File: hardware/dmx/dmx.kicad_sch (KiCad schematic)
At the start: 67 parts, among them J1 Midi In, J2 Midi Thru, J3 NeoPixel, J4 Power, J5 DMX, J6 I2C0, J7 I2C1, Q1 BSS138, Q2 BSS138, Q3 TSM680P06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

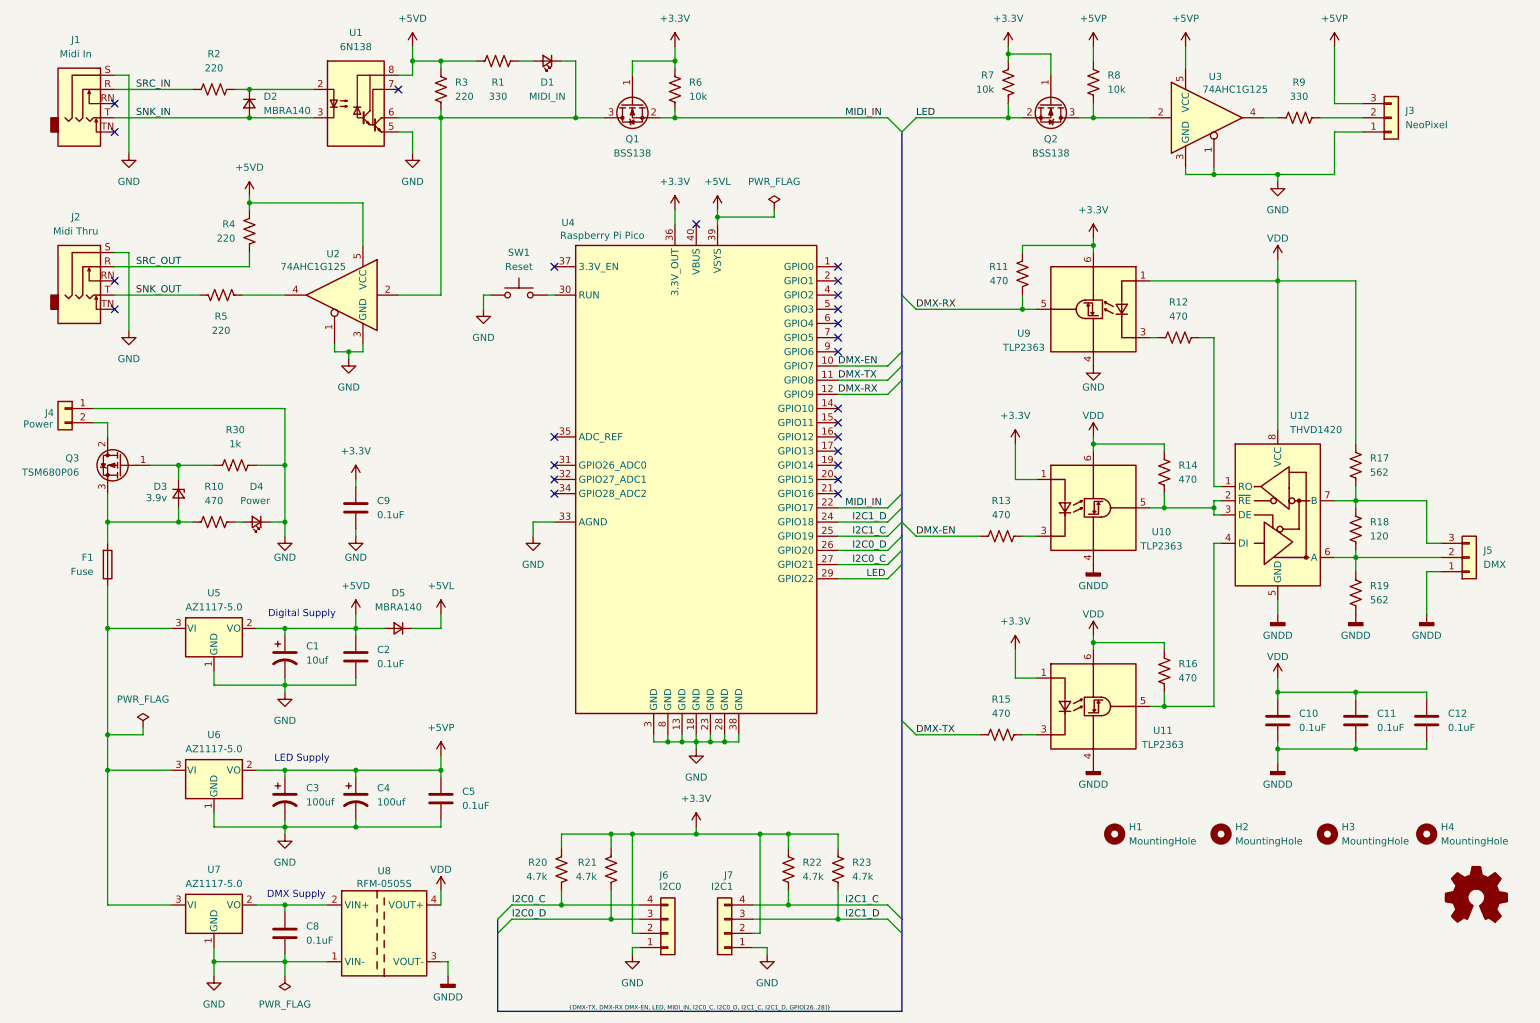
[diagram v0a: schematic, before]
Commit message: Rev 1.1: - Update to latest KiCad - Fixed short in servo board - Updates to right-angle diag connector on servo boards - Fixed microproc footprint on diag board - Flipped I2C connector to top of diag board - Pass all ERC and DRC checks, add exclusions
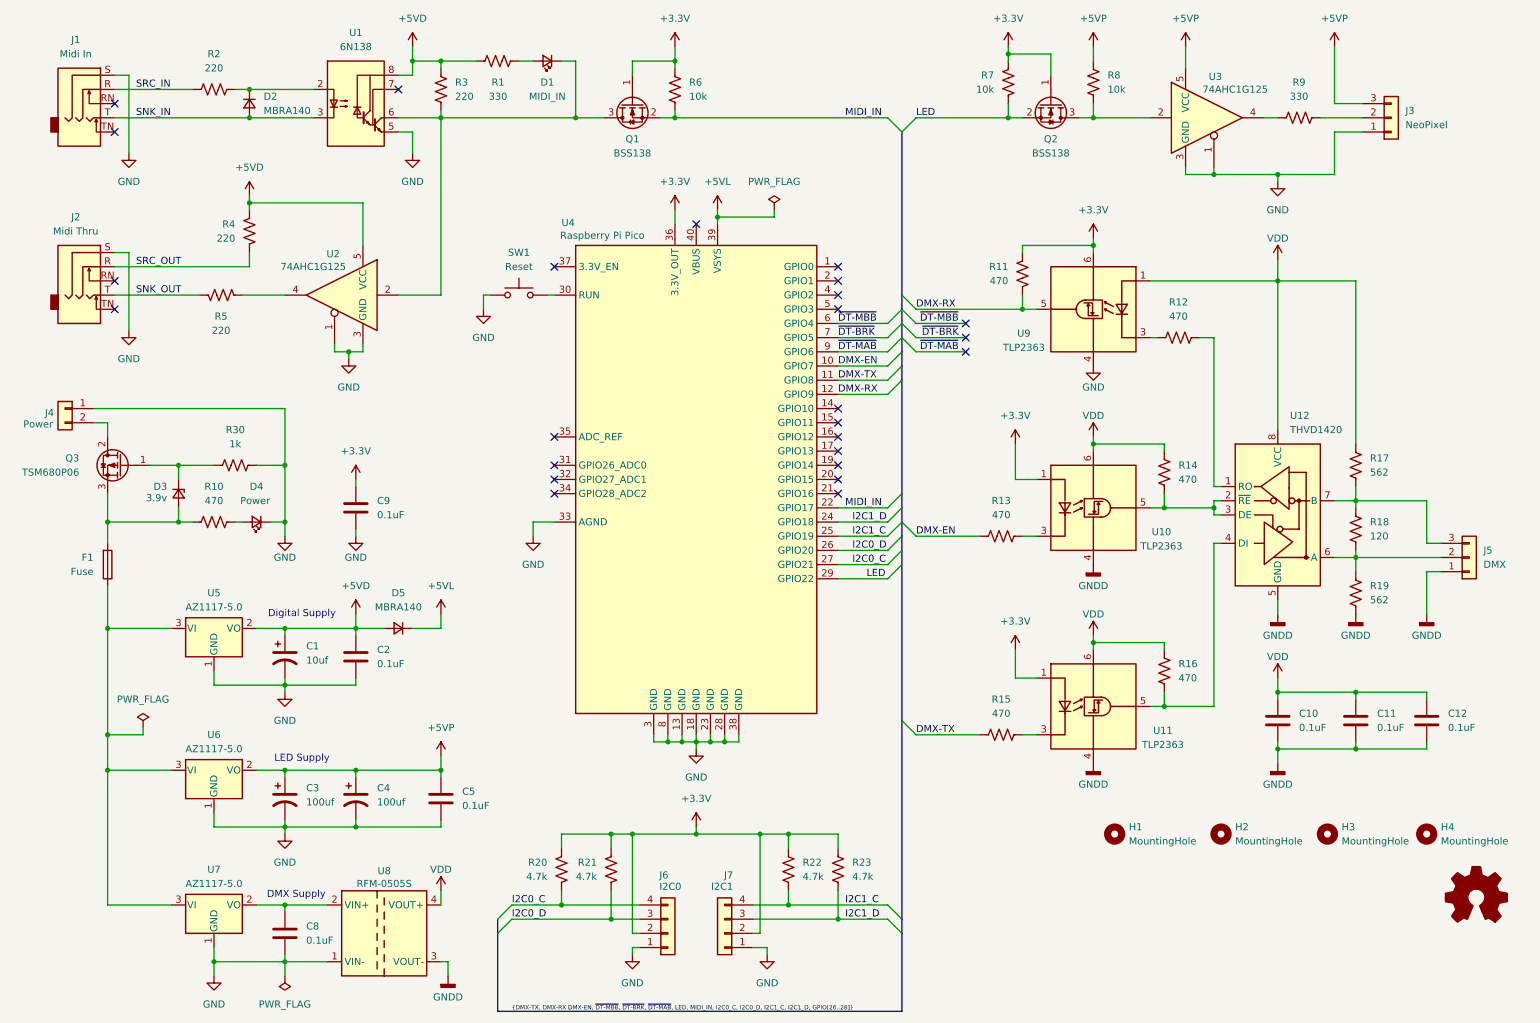
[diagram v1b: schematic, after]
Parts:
- Q3: symbol Device:Q_PMOS_GDS -> Transistor_FET:Q_PMOS_GDS
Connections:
- net ~{DT-MBB}: now reaches U4.6 (GPIO4)
- net ~{DT-BRK}: now reaches U4.7 (GPIO5)
- net ~{DT-MAB}: now reaches U4.9 (GPIO6)
